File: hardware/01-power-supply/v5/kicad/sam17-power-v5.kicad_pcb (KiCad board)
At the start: 4 copper layers, 200 x 150 mm, 212 parts, among them J1 Bornera 2P 5.0 mm, J10 PinHeader 1x04, J2 Molex KK-254 4P, J3 Bornera 4P 5.08 mm, J5 Faston 6.3x0.8 PCB, J6 Molex KK-254 2P, J7 Molex KK-254 4P, J8 PinHeader 1x04, J9 Molex KK-254 2P, Q2 CSD18534Q5A, Q3 MMBT3906, Q4 MMBT3906, Q5 MMBT3906, Q6 MMBT3906, SW1 Pulsador 6x6, U1 LT1963AEQ, U10 ADS1115IDGS, U11 TMP1075DGK, U12 INA226, U13 INA226, U14 INA226, U15 LM74502DDFR, U16 TPS26631PWPR, U17 MSP430FR2111IPW16, U18 TPS70933DBVR, U19 TPS26631PWPR, U2 LT3015EQ, U20 LM393B, U21 TL431BI, U22 TL431BI, U23 TL431BI, U24 TL431BI, U25 TL431BI, U4 LT3045EDD, U5 LT3045EDD, U6 LT3094EDD, U7 LT3094EDD, U8 INA226, U9 ISO1541

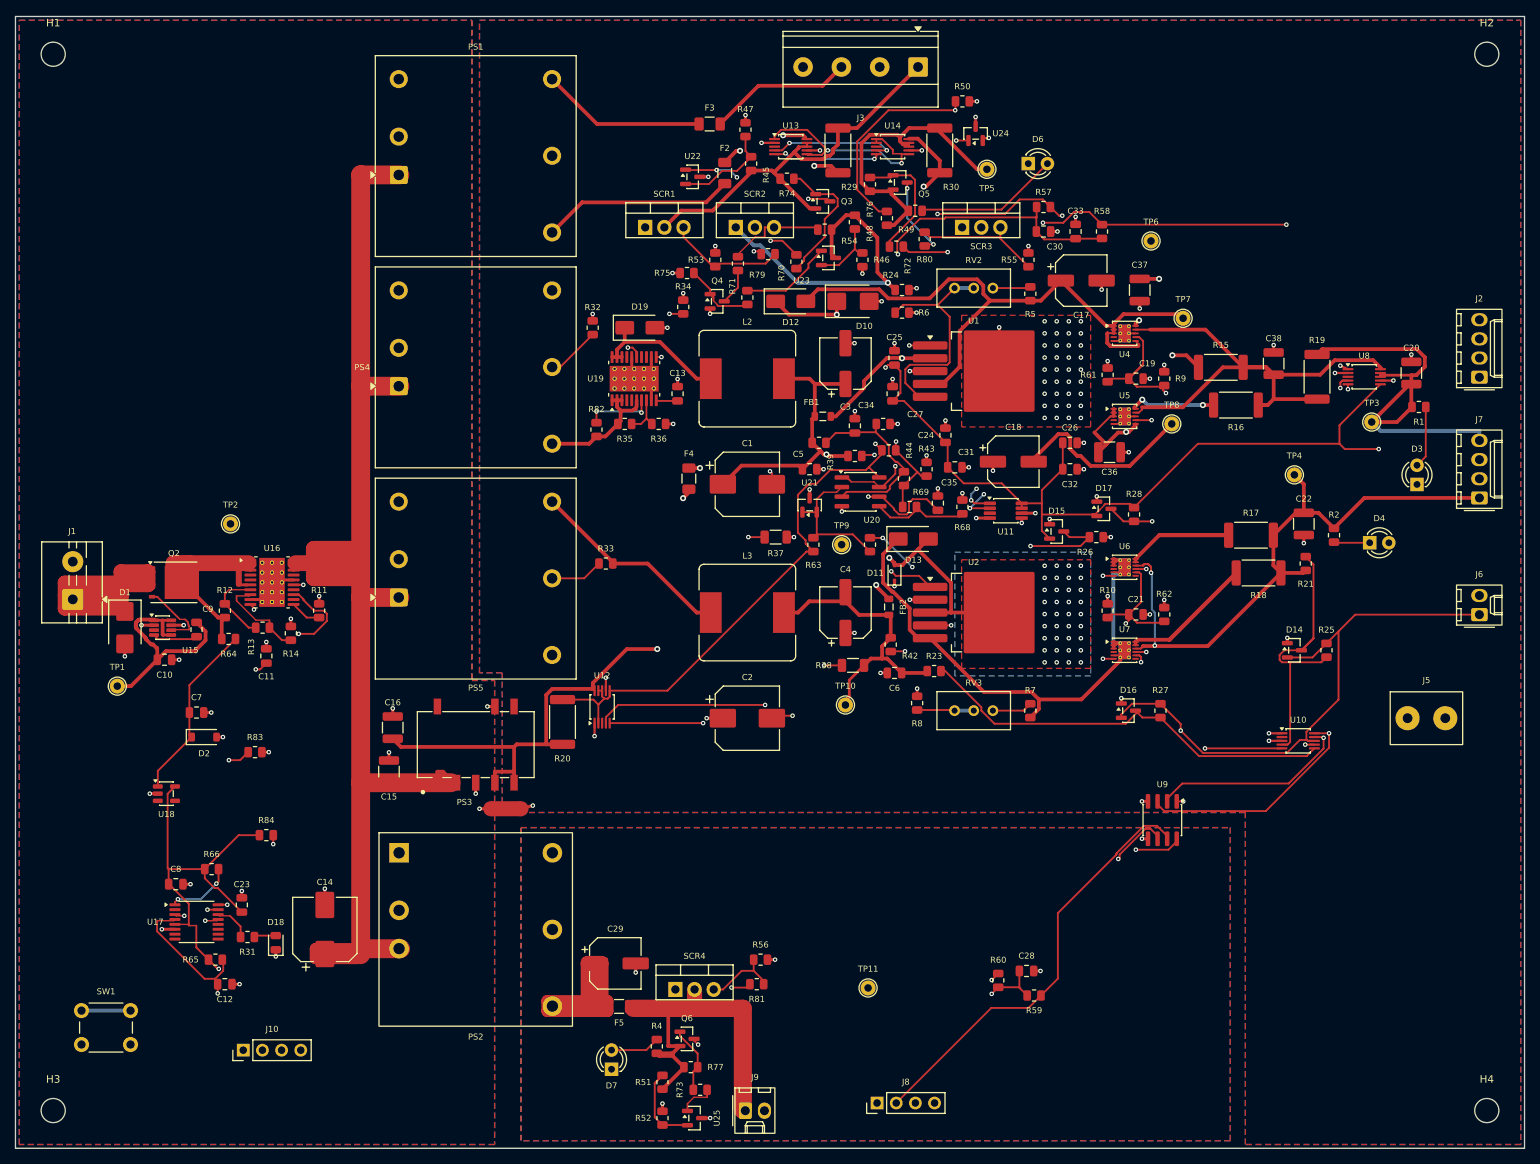
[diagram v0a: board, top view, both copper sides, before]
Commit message: hardware: fuente v5, placa y fabricacion con L2 en SRP1265A-220M
Placa colocada y ruteada de nuevo: Freerouting en 3 rondas y el rescate
cierra las 7 conexiones que deja abiertas. L2 sigue en (97, 48); su
cuerpo pasa de 12,5 a 13,5 mm en x.

build_pcb.py: Freerouting salio de U4.9 por su cuenta y puso la via a
mitad de la salida fija de OUTS_POS, con 0,8 mm de punta colgando.
limpiar_colgantes() ya no deja asi una pista fija: la recorta hasta el
ultimo contacto de su red (_recortar), y lo de antes no cambia.

- 1510 pistas y 284 vias (263 de 0,6/0,3 mm y 21 de 0,8/0,4 mm).
- Bajo el cuerpo de L2 pasan ahora +15V5_FILT en F.Cu, entre sus pads, y
  SCL_A/SDA_A en In2, debajo del plano de In1.
- DRC (kicad-cli 10.0.3, todas las severidades, zonas rellenas y paridad
  con el esquematico): 0 infracciones, 0 sin conectar, 0 de paridad.
- Ocho referencias van solo en F.Fab: entran R43, R70, R71 y FB1, y R40
  y R67 vuelven a la serigrafia.

Esquematico, netlist, fab/ y pcb/ regenerados.
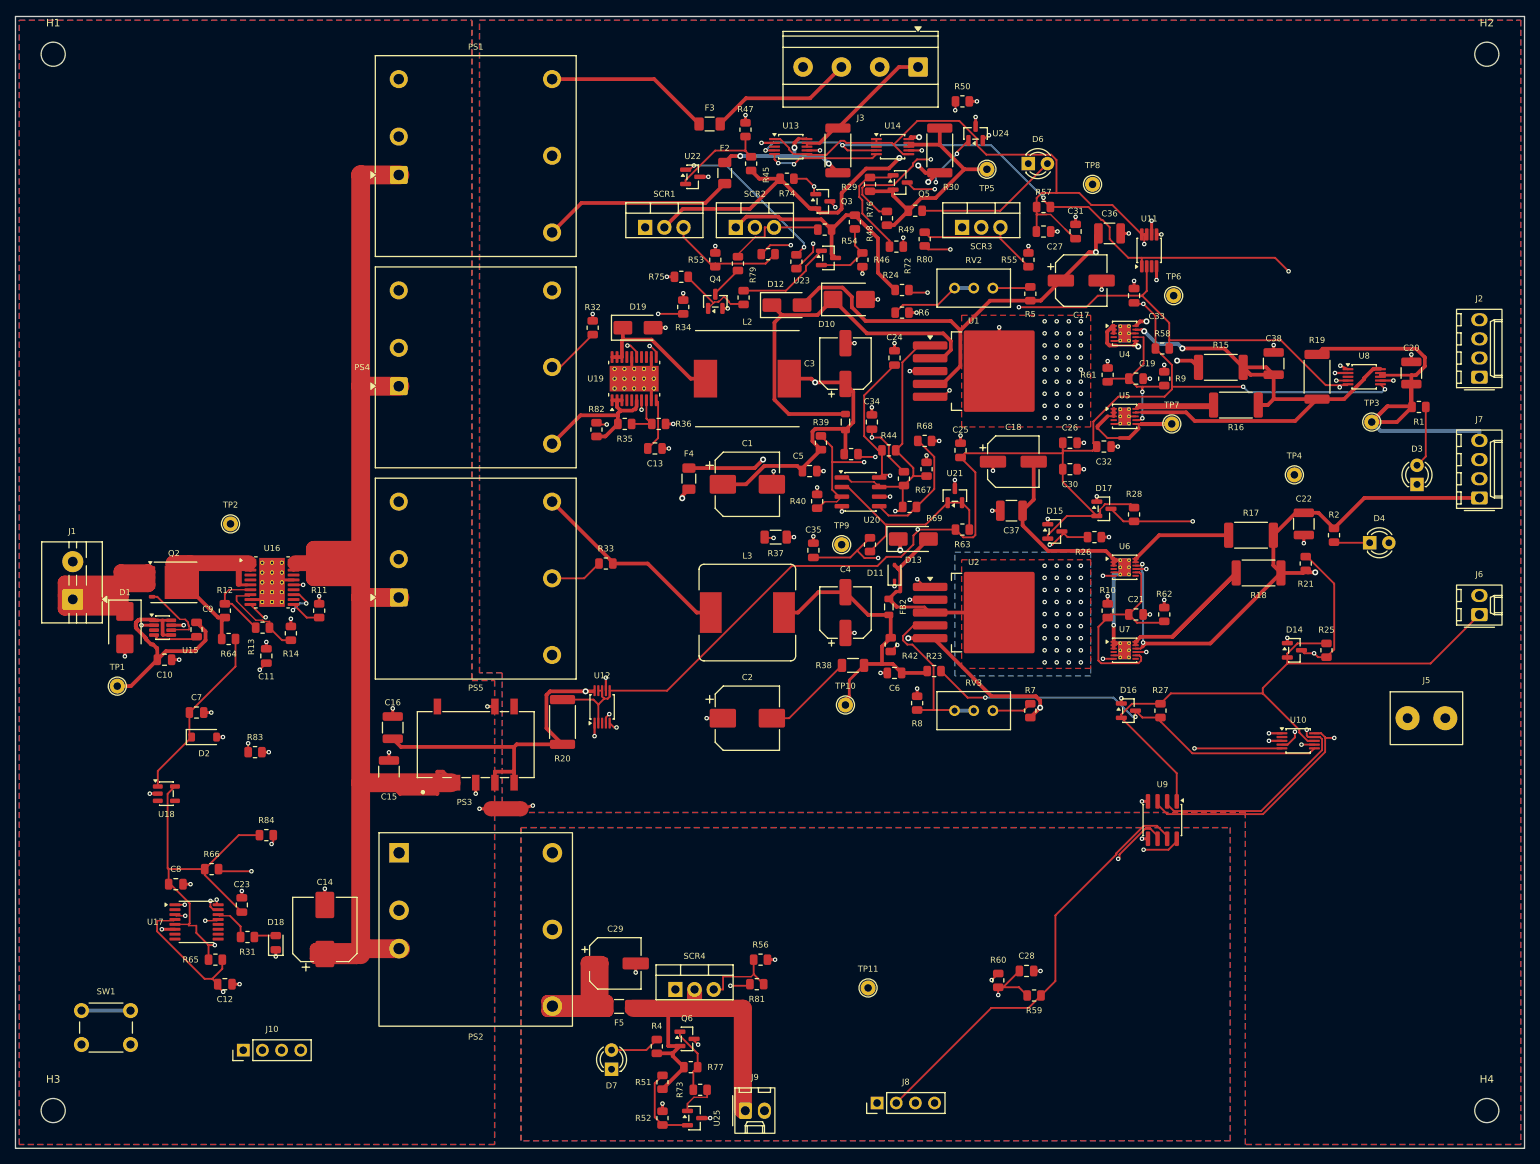
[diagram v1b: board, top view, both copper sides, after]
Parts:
- L2: value 22uH SRR1260-220M -> 22uH SRP1265A-220M; footprint Inductor_SMD:L_Bourns_SRR1260 -> sam17:L_Bourns_SRP1265A
- moved U11 39.4 mm to (150.2, 31.0), turned to 90 degrees
- moved C31 35.1 mm to (140.5, 28.5), turned to 90 degrees
- moved C37 33.8 mm to (132.0, 65.5), turned to 0 degrees
- moved TP8 33.4 mm to (142.7, 22.2)
- moved C30 31.7 mm to (139.8, 60.0)
- moved C27 29.4 mm to (136.2, 28.5), turned to 0 degrees
- moved C36 29.0 mm to (145.0, 28.8)
- moved R63 19.9 mm to (125.5, 68.0), turned to 0 degrees
- moved U21 19.3 mm to (124.5, 63.5)
- moved C35 17.6 mm to (105.8, 70.8)
- moved R58 17.4 mm to (152.0, 44.0), turned to 0 degrees
- moved C25 15.1 mm to (125.2, 57.5)
- moved TP7 14.1 mm to (153.2, 54.0)
- moved R40 13.5 mm to (106.2, 64.2), turned to 90 degrees
- moved C24 12.3 mm to (116.5, 45.2)
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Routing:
- net +12V_RACK: track 55.2 -> 76.7 mm, vias 0 -> 1
- net +5V_AUX: track 401.4 -> 420.8 mm, vias 8 -> 6
- net SHDN_CASCADE: track 67.9 -> 49.8 mm, vias 4 -> 2
- net +15V5_FILT: track 38.6 -> 53.6 mm, vias 2 -> 0
- net +15V5_LC: track 49.8 -> 64.1 mm
- net OUT_U7: track 30.1 -> 41.5 mm
- net -12V_RACK: track 95.7 -> 86.3 mm, vias 1 -> 0
- net OUT_U5: track 11.5 -> 20.8 mm, vias 2 -> 0
- net OUT_U6: track 23.3 -> 14.1 mm
- net SCL_A: track 287.8 -> 278.8 mm, vias 9 -> 6
- net -12V_ULTRA: track 99.3 -> 108.0 mm, vias 2 -> 3
- net VREF_2V5: track 19.2 -> 27.6 mm
- net +24V_SW: track 188.1 -> 196.4 mm
- net OUTS_POS: track 70.5 -> 77.6 mm, vias 0 -> 2
- net SDA_A: track 272.5 -> 265.4 mm, vias 9 -> 7
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
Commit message: fix(fuente-v5): PS3 a THN 20-2411WI aislado, con C39 y +5V_AUX tras F4
El K7805T de PS3 era un buck no aislado: con la entrada puenteada a la
salida, +5V_AUX pasaba de los 6,0 V de los INA226 y del ISO1541. En el
THN 20-2411WI la entrada y la salida solo se tocan por la barrera de
1600 VDC, el camino que la propuesta de piezas (sec. 9.1) deja fuera del
contrato de fallo simple.

- C39, 1000 uF / 16 V (Lelon VZH102M1CTR-1010, C249844): con el THN a su
  limite la subida del riel baja a 0,0095 V/us y el pico queda en 5,88 V.
- +5V_AUX cuelga de +5V_FUSED_RACK: si F4 abre tras el disparo, se apaga
  en vez de quedarse con el OVP del THN (hasta 8,20 V).
- R49 = 12,7 kohm: SCR3 dispara entre 5,53 y 5,86 V.
- check_absmax.py: fuga_ps3() con su guarda y sus canarios, y la fila de
  +5V_AUX en absmax.csv. check_netlist.py fija la toma de R20 tras F4.
- Placa reruteada: PS3 en la columna de convertidores, PS2 abajo, NT1
  entre PS5 y PS3, GNDA por la derecha de PS3 y C39. DRC 0, 0 sin conectar.
- Presupuestos: derating del 2411WI, 83 % al 20 % de carga (el cajon pasa
  a 65,31 W), medidas.csv.
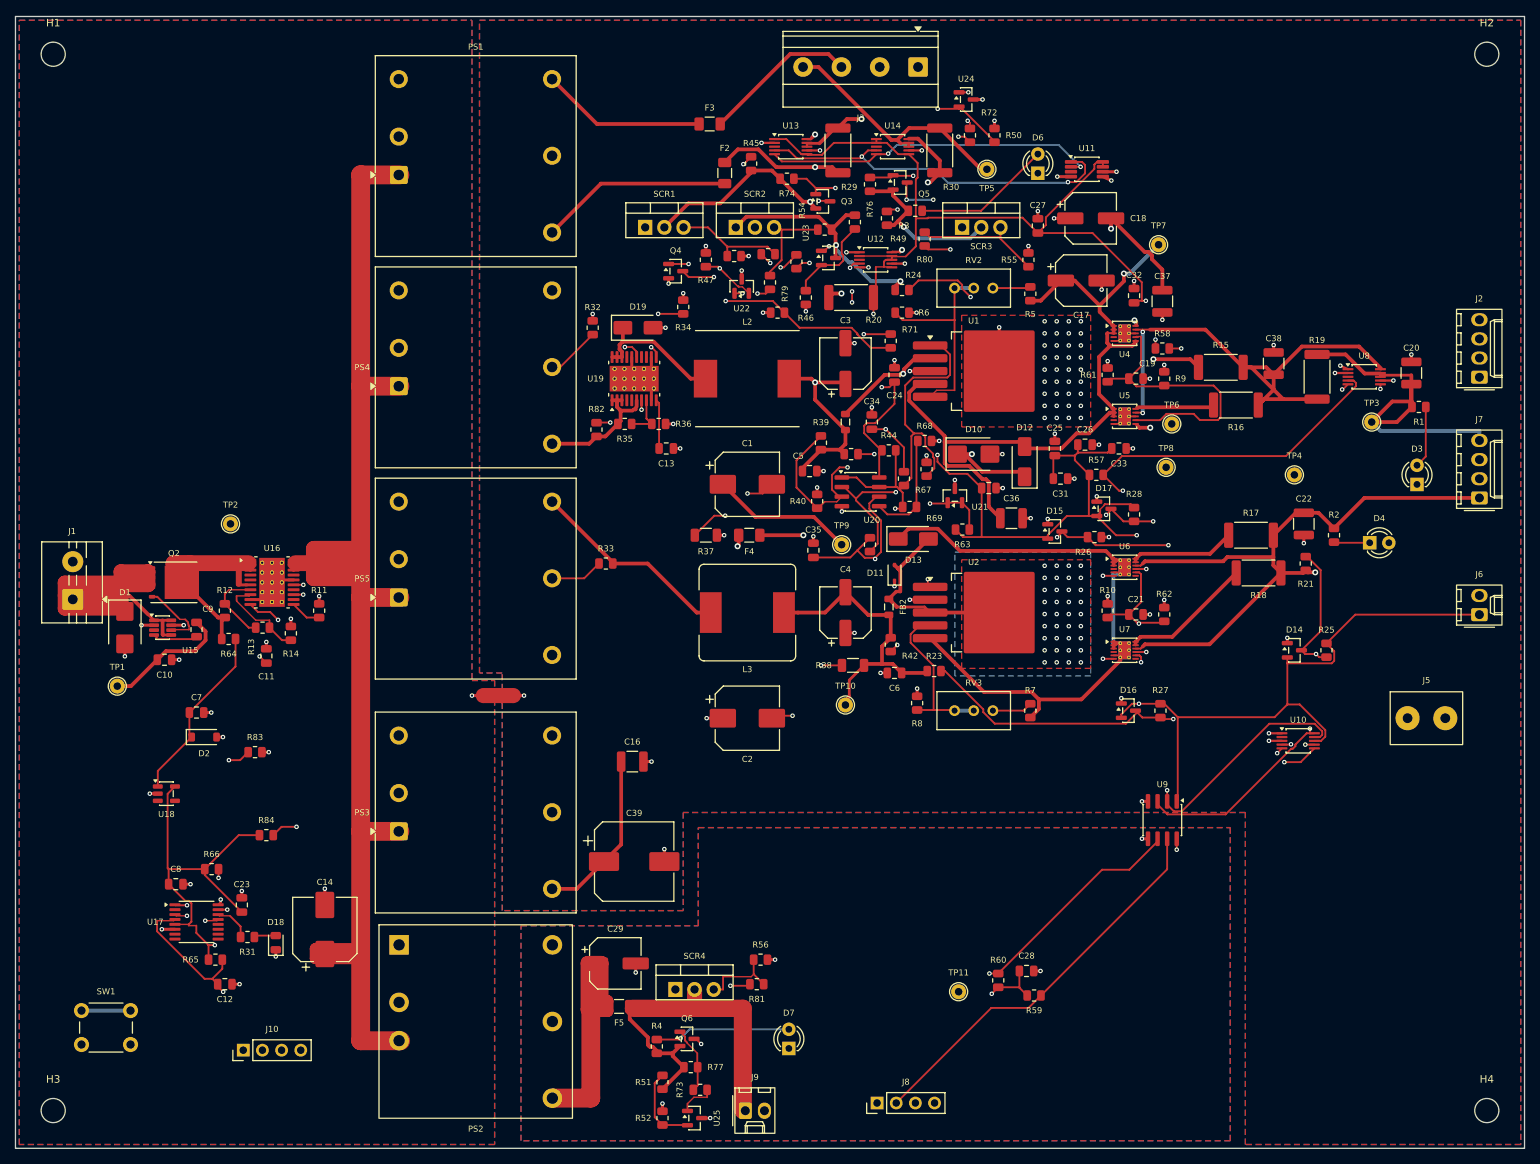
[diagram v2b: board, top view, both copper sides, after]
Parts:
- removed C15: 10uF 50V X7R, Capacitor_SMD:C_1210_3225Metric
- added C39: 1000uF 16V, Capacitor_SMD:CP_Elec_10x10, F.Cu at (82.0, 112.0)
- PS3: value K7805T-1000R3 -> THN 20-2411WI; footprint sam17:Converter_DCDC_Mornsun_K78_T-1000R3_SMD -> Converter_DCDC:Converter_DCDC_TRACO_THL30-xxxxWI_THT
- R49: value 13.3k 0.1% -> 12.7k 0.1%
- moved U12 69.5 mm to (114.0, 32.2), turned to 0 degrees
- moved R20 68.0 mm to (110.8, 37.2), turned to 0 degrees
- moved C36 39.9 mm to (132.0, 66.5)
- moved TP8 38.7 mm to (152.5, 59.8)
- moved D12 37.7 mm to (133.8, 59.0), turned to 90 degrees
- moved R57 36.2 mm to (143.2, 60.8)
- moved C37 34.2 mm to (152.0, 37.8), turned to 90 degrees
- moved C18 33.8 mm to (142.5, 26.8)
- moved C31 32.8 mm to (138.5, 61.2), turned to 0 degrees
- moved C16 32.1 mm to (81.8, 98.8), turned to 0 degrees
- moved D10 26.3 mm to (127.0, 58.0)
- moved TP7 23.8 mm to (151.5, 30.2)
- moved D7 23.7 mm to (102.5, 136.8)
- moved C32 20.4 mm to (148.2, 37.0), turned to 90 degrees
- moved C33 20.3 mm to (146.2, 57.2), turned to 0 degrees
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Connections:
- C16 pad 2: GND24 -> GNDA
- PS3 pad 2: +24V_SW -> GND24
- PS3 pad 3: GND24 -> +5V_RAW_RACK
- PS3 pad 4: +5V_RAW_RACK -> unconnected-(PS3-Trim-Pad4)
- PS3 pad 5: +5V_RAW_RACK -> GNDA
- R20 pad 1: +5V_RAW_RACK -> +5V_FUSED_RACK
- U12 pad 10: +5V_RAW_RACK -> +5V_FUSED_RACK
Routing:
- net SCL_A: track 278.8 -> 189.6 mm
- net +5V_AUX: track 420.8 -> 361.8 mm, vias 6 -> 8
- net SDA_A: track 265.4 -> 225.3 mm, vias 7 -> 5
- net OUT_U7: track 41.5 -> 17.6 mm
- net QB_CB2: track 10.7 -> 34.1 mm, vias 0 -> 2
- net +12V_RACK: track 76.7 -> 58.7 mm, vias 1 -> 2
- net SET_POS: track 20.8 -> 38.4 mm, vias 2 -> 0
- net AIN3: track 109.6 -> 92.8 mm, vias 3 -> 4
- net SHDN_CASCADE: track 49.8 -> 64.3 mm
- net +15V5_FILT: track 53.6 -> 41.1 mm, vias 0 -> 2
- net +12V_ULTRA: track 79.1 -> 67.2 mm
- net TLK_CB1: track 22.2 -> 10.3 mm
- net TLK_CB3: track 17.7 -> 6.18 mm, vias 3 -> 2
- net LED7_A: track 6.58 -> 18.1 mm, vias 0 -> 1
- net REF_CB1: track 13.1 -> 23.7 mm, vias 0 -> 2
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
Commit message: feat(fuente-v5): placa y ficheros de fabricacion con Q7 en el retorno
Regenerados con build_schematic.py, build_pcb.py y build_fab.py: DRC con
todas las severidades y paridad con el esquematico en 0 infracciones, 0 sin
conectar y 0 diferencias de paridad; 1464 pistas y 294 vias (271 de 0,6 mm y
23 de 0,8 mm).

- Q7 sobre J1.2 (rot 270, drenador abajo) y D1 a su lado; la isla
  RET24_RAW (J1.2, D1.2 y el drenador de Q7) es cobre fijo de >= 2,4 mm que
  los vertidos de GND24 rodean sin tocar, y las tres fuentes de Q7 van
  juntas a GND24 por cobre de 1,8 mm. R85 y D20 quedan junto a D1.
- L3 en la huella de la SRP1265A (13,5 x 12,5 mm).
- fab/: gerbers, taladros y posiciones; el BOM y el CPL de JLC pierden D10 y
  D12 (sin montar) y ganan Q7, D20 y R85. Nueve referencias solo en F.Fab.
- sam17-power-v5.net, .kicad_sch, esquemas y vistas de la placa.
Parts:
- added D20: BZT52C15, Diode_SMD:D_SOD-123, F.Cu at (22.5, 65.0)
- added Q7: CSD18534Q5A, Package_TO_SOT_SMD:TDSON-8-1, F.Cu at (7.60, 64.5)
- added R85: 10k, Resistor_SMD:R_0805_2012Metric, F.Cu at (19.0, 68.0)
- C10: value 100nF 50V X7R -> 100nF 100V X7R
- D1: value SMBJ26CA -> SMBJ33CA
- L3: value 22uH SRR1260-220M -> 22uH SRP1265A-220M; footprint Inductor_SMD:L_Bourns_SRR1260 -> sam17:L_Bourns_SRP1265A
- R32, R33: value 45.3k -> 45.3k 0.1%
- R64: value 1k -> 1.2k
- moved R63 32.8 mm to (92.8, 69.2), turned to 90 degrees
- moved C32 32.8 mm to (129.0, 63.5)
- moved C27 30.4 mm to (141.8, 57.5)
- moved C26 29.7 mm to (135.5, 27.8), turned to 90 degrees
- moved C31 26.1 mm to (148.2, 37.0), turned to 90 degrees
- moved C25 23.4 mm to (116.5, 47.5)
- moved C24 23.1 mm to (137.8, 56.5), turned to 0 degrees
- moved U21 20.6 mm to (104.8, 69.2), turned to 0 degrees
- moved C35 17.6 mm to (122.2, 64.5)
- moved D1 12.9 mm to (15.0, 68.2), turned to 90 degrees
- moved R68 10.1 mm to (125.5, 65.0), turned to 90 degrees
- moved R12 9.53 mm to (28.5, 69.2), turned to 0 degrees
- moved C9 9.30 mm to (14.8, 82.2)
- moved C30 9.10 mm to (137.8, 60.0)
- moved TP1 7.95 mm to (21.2, 87.0)
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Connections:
- D1 pad 2: GND24 -> RET24_RAW
- J1 pad 2: GND24 -> RET24_RAW
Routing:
- net +5V_AUX: track 361.8 -> 407.1 mm, vias 8 -> 9
- net +13V1: track 123.7 -> 99.8 mm, vias 2 -> 3
- net G_Q7: track 0.00 -> 19.3 mm
- net SCL_A: track 189.6 -> 207.8 mm
- net +15V5_LC: track 67.8 -> 50.9 mm, vias 1 -> 2
- net +24V_RAW: track 87.0 -> 70.1 mm
- net -12V9: track 157.1 -> 140.9 mm, vias 1 -> 3
- net RET24_RAW: track 0.00 -> 14.0 mm
- net SDA_A: track 225.3 -> 238.9 mm, vias 5 -> 8
- net SHDN_CASCADE: track 64.3 -> 51.6 mm
- net AIN3: track 92.8 -> 103.4 mm, vias 4 -> 3
- net -12V_ULTRA: track 114.8 -> 105.5 mm, vias 1 -> 0
- net OUT_U6: track 14.1 -> 23.3 mm
- net QB_CB3: track 15.8 -> 24.5 mm, vias 2 -> 0
- net GATE_SCR1: track 14.8 -> 23.2 mm, vias 0 -> 1
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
